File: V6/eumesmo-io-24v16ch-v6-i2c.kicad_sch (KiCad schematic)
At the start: 26 parts, among them J9 250-203, SW2 1WIRE_SEL, U10 MCP23017, U11 DS2482S-100, U8 MCP23008, U9 MCP23008

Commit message: Renamed all files to eumesmo branding
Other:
- title: ESP 24V 16xIn/16xOut/1-Wire Module -> eumesmo 24V 16xIn/16xOut/1-Wire Module

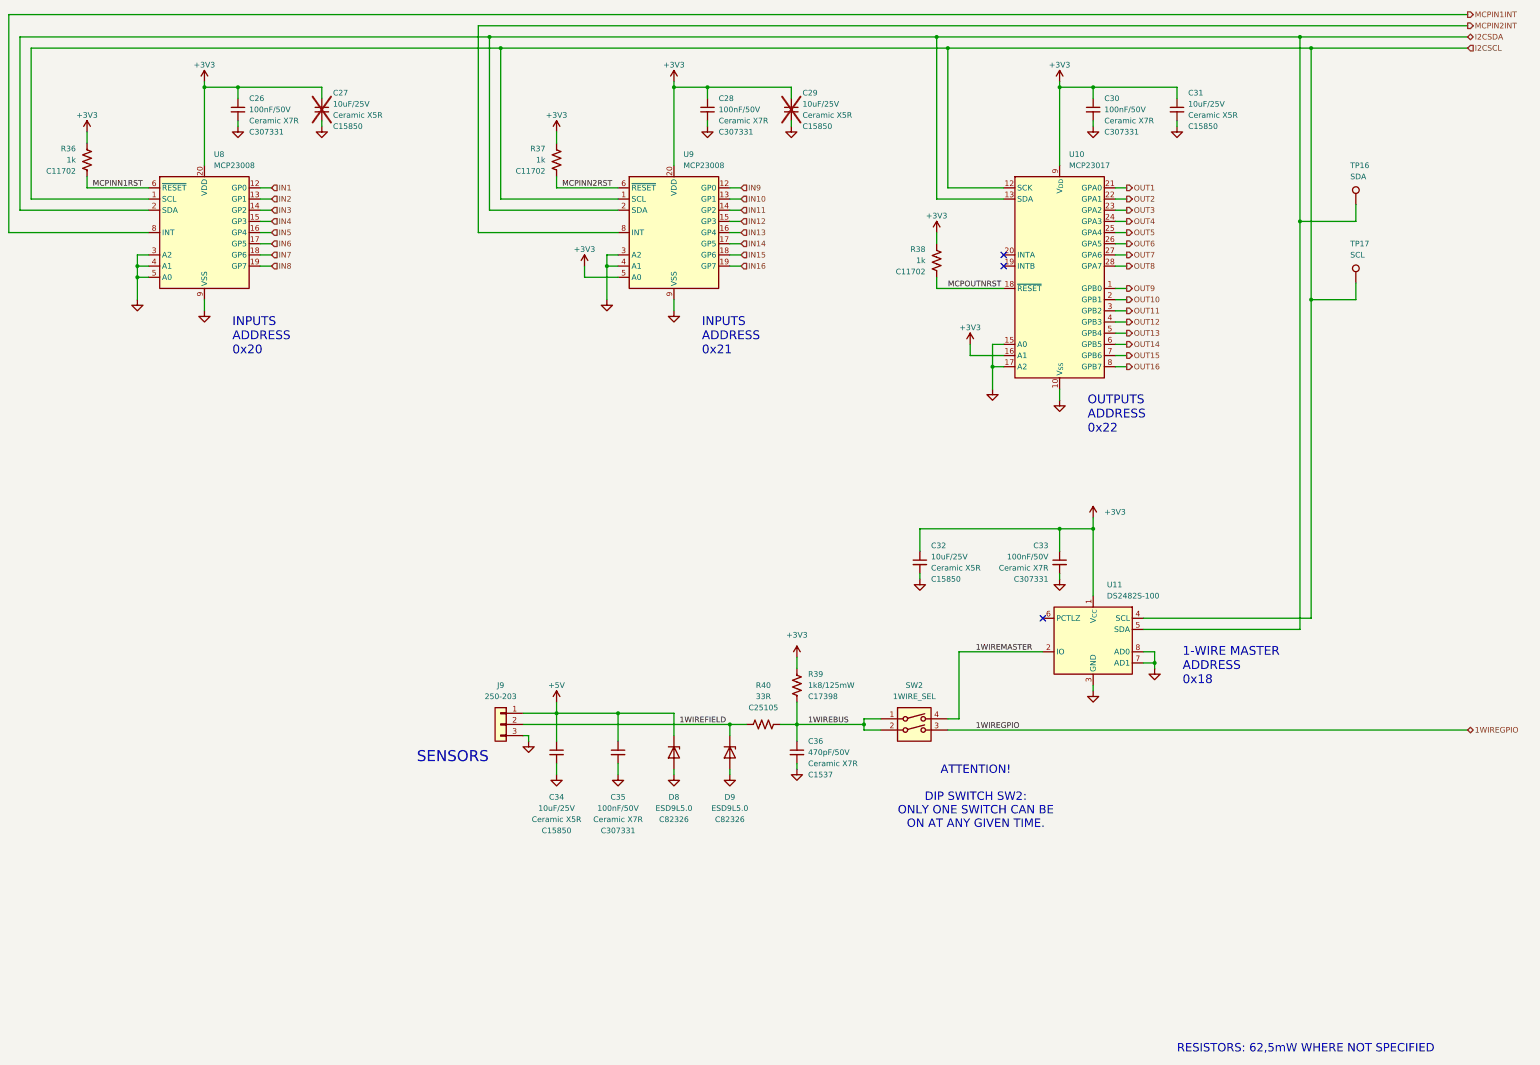
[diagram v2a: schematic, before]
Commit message: Added CPU health LED
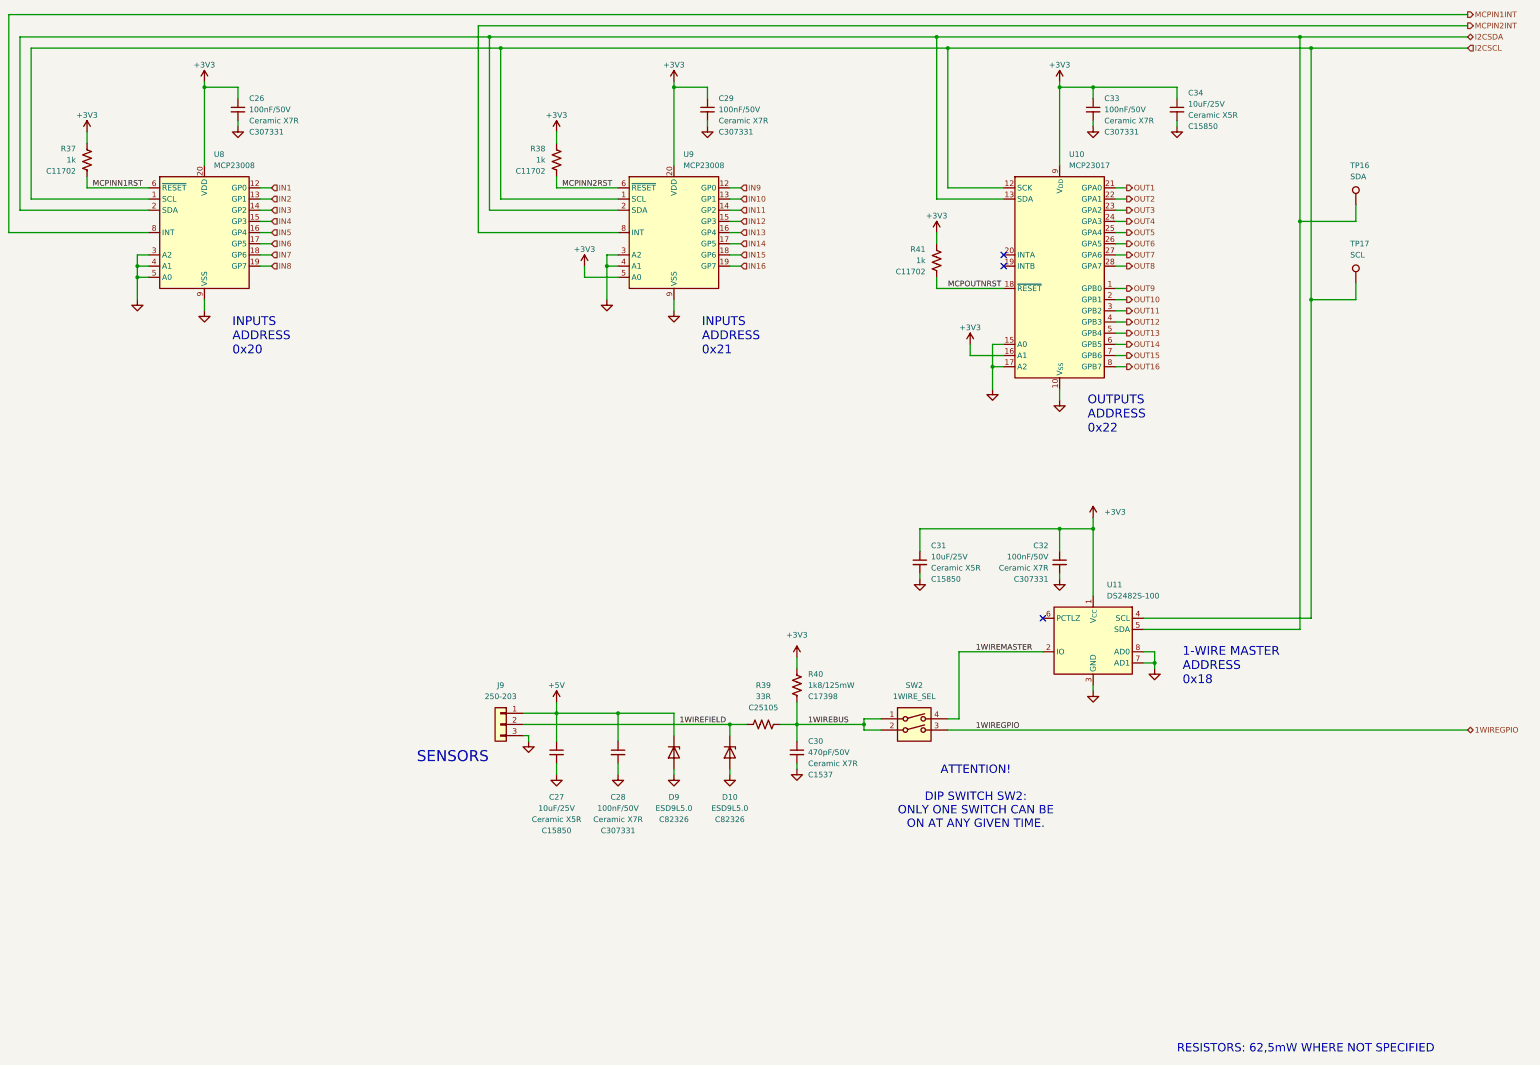
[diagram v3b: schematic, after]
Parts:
- removed C27, C29: 10uF/25V, Tales:C_0805_2012Metric, symbol Device:C_Small
- renumbered C34 to C27, C35 to C28, C28 to C29, C36 to C30, C32 to C31, C33 to C32, C30 to C33, C31 to C34, D9 to D10, D8 to D9, R36 to R37, R37 to R38, R40 to R39, R39 to R40, R38 to R41
